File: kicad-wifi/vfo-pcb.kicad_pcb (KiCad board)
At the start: 2 copper layers, 108.4 x 79.9 mm, 110 parts, among them J1 Rotery Encoder1, J10 Link-out 1-2, J11 Link-out 1-0, J12 Link-out 2-0, J13 Link-out 2-2, J14 Link-out 2-1, J15 Link-out 1-1, J16 JTAG, J17 I2C, J2 Rotery Encoder2, J3 Analog in 3-6, J4 RxTx, J5 V12, J6 ESP32L, J7 ESP32R, J8 ILI9341, J9 Conn_01x07_Female, Q1 BFR92, Q2 BFR92, Q3 BFR92, Q4 BFR92, Q5 BFR92, Q6 BFR92, SW1 Rotary_Encoder_Switch, U1 AMS1117, U2 LM2576HVS-ADJ, U3 Si5351A-B-GT, U4 Si5351A-B-GT, U5 PCF8574ATS, Y1 Crystal, Y2 Crystal

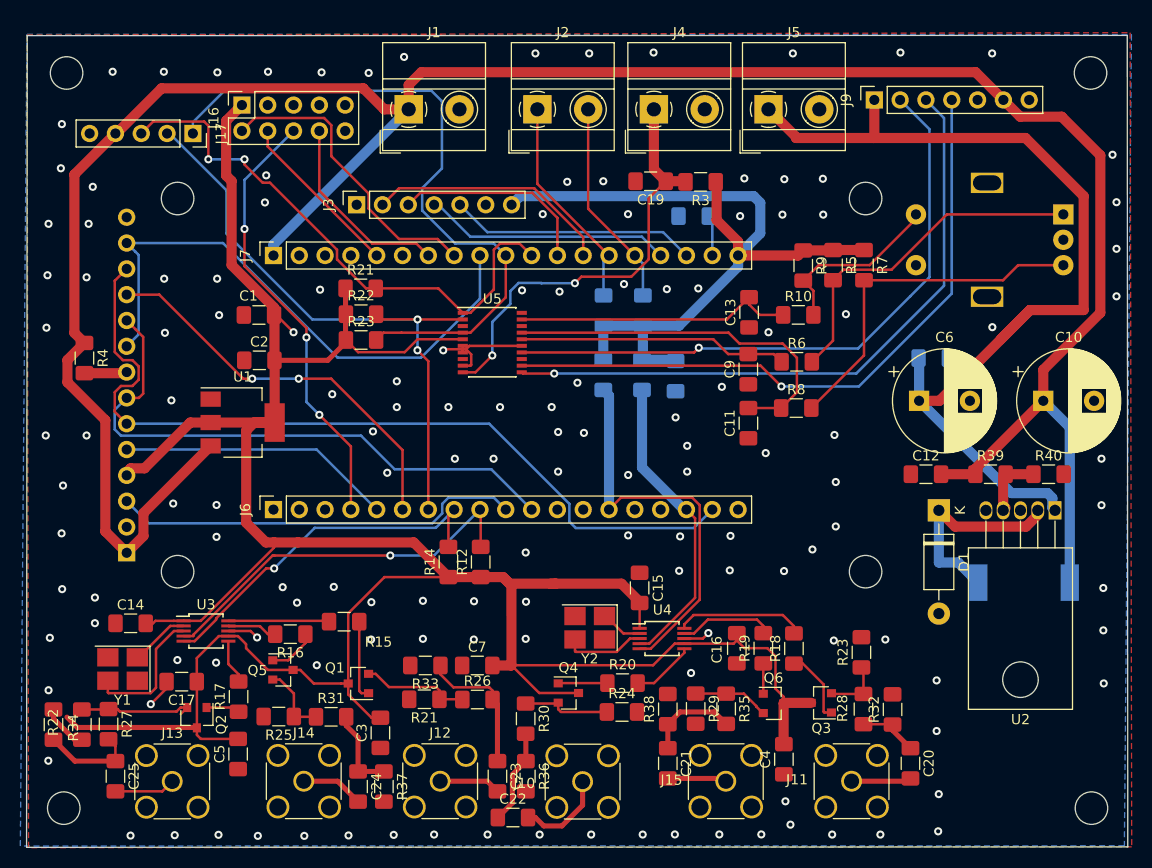
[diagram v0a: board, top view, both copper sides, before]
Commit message: 4 layer PCB
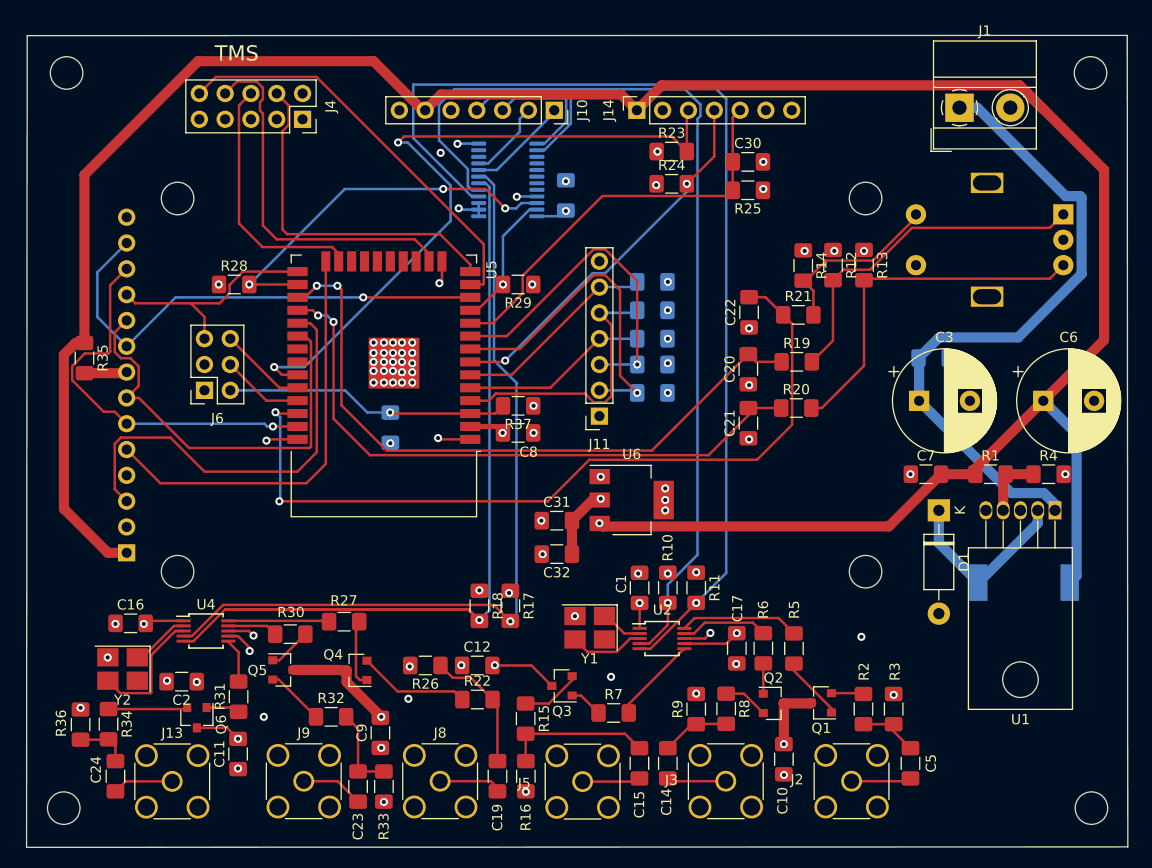
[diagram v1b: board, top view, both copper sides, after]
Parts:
- removed the C18 at (106.2, 85.9)
- removed the C2 at (65.2, 84.3)
- removed the J1 at (79.9, 59.6)
- removed J16: JTAG, Connector_PinSocket_2.54mm:PinSocket_2x05_P2.54mm_Vertical
- removed the J2 at (92.6, 59.6)
- removed J7: ESP32R, Connector_PinSocket_2.54mm:PinSocket_1x19_P2.54mm_Vertical
- removed the J9 at (125.7, 58.7)
- removed the R21 at (75.2, 77.2)
- removed the R21 at (81.5, 117.7)
- removed the R22 at (47.8, 120.1)
- removed the R23 at (75.2, 82.3)
- removed the R23 at (124.5, 113.0)
- removed the R24 at (100.9, 118.9)
- removed the R25 at (67.1, 119.3)
- removed the R32 at (127.5, 118.7)
- removed R38: 150, Resistor_SMD:R_1206_3216Metric_Pad1.42x1.75mm_HandSolder
- removed the U1 at (63.6, 90.4)
- added C13: 100n, Capacitor_SMD:C_1206_3216Metric_Pad1.42x1.75mm_HandSolder, B.Cu at (95.4, 68.1)
- added C25: 100n, Capacitor_SMD:C_1206_3216Metric_Pad1.42x1.75mm_HandSolder, B.Cu at (103.9, 76.6)
- added C26: 100n, Capacitor_SMD:C_1206_3216Metric_Pad1.42x1.75mm_HandSolder, B.Cu at (103.9, 79.4)
- added C27: 100n, Capacitor_SMD:C_1206_3216Metric_Pad1.42x1.75mm_HandSolder, B.Cu at (103.9, 82.2)
- added C28: 100n, Capacitor_SMD:C_1206_3216Metric_Pad1.42x1.75mm_HandSolder, B.Cu at (103.9, 87.5)
- added C29: 100n, Capacitor_SMD:C_1206_3216Metric_Pad1.42x1.75mm_HandSolder, B.Cu at (103.9, 84.7)
- added C31: 100n, Capacitor_SMD:C_1206_3216Metric_Pad1.42x1.75mm_HandSolder, F.Cu at (94.5, 100.1)
- added C32: 10u, Capacitor_SMD:C_1206_3216Metric_Pad1.42x1.75mm_HandSolder, F.Cu at (94.5, 103.4)
- added J14: Encoders, Connector_PinSocket_2.54mm:PinSocket_1x07_P2.54mm_Vertical, F.Cu at (102.4, 59.7)
- added R3: 68, Resistor_SMD:R_1206_3216Metric_Pad1.42x1.75mm_HandSolder, F.Cu at (127.6, 118.6)
- added R37: 1k, Resistor_SMD:R_1206_3216Metric_Pad1.42x1.75mm_HandSolder, F.Cu at (90.7, 88.8)
- added R9: 68, Resistor_SMD:R_1206_3216Metric_Pad1.42x1.75mm_HandSolder, F.Cu at (108.2, 118.6)
- added U3: TCA9548APWR, Package_SO:TSSOP-24_4.4x7.8mm_P0.65mm, B.Cu at (89.7, 66.5)
- added U6: LM1117-3.3, Package_TO_SOT_SMD:SOT-223-3_TabPin2, F.Cu at (101.9, 98.0)
- C20: renamed from C9; value 10n -> 100n
- C21: renamed from C11; value 10n -> 100n
- C22: renamed from C13; value 10n -> 100n
- J10: renamed from J17; footprint Connector_PinSocket_2.54mm:PinSocket_1x05_P2.54mm_Vertical -> Connector_PinSocket_2.54mm:PinSocket_1x07_P2.54mm_Vertical
- J4: value RxTx -> Jtag; footprint TerminalBlock_MetzConnect:TerminalBlock_MetzConnect_Type011_RT05502HBWC_1x02_P5.00mm_Horizontal -> Connector_PinSocket_2.54mm:PinSocket_2x05_P2.54mm_Vertical
- J6: value ESP32L -> Prog; footprint Connector_PinSocket_2.54mm:PinSocket_1x19_P2.54mm_Vertical -> Connector_PinSocket_2.54mm:PinSocket_2x03_P2.54mm_Vertical
- R10: renamed from R11; moved to F.Cu
- R11: renamed from R13; moved to F.Cu
- R15: renamed from R30; value 33 -> 200
- R16: renamed from R36; value 150 -> 68
- R2: renamed from R28; value 33 -> 200
- R23: renamed from R1; moved to F.Cu
- R24: renamed from R2; moved to F.Cu
- R29: value 150 -> 2.2k
- R8: renamed from R35; value 33 -> 200
- U5: value PCF8574ATS -> ESP32-WROOM-32D; footprint Package_SO:SSOP-20_4.4x6.5mm_P0.65mm -> RF_Module:ESP32-WROOM-32
- moved R29 45.2 mm to (90.7, 76.8), turned to 180 degrees
- moved C18 36.4 mm to (78.1, 90.9), turned to 270 degrees
- moved J10 35.6 mm to (94.2, 59.7)
- moved J4 34.6 mm to (69.5, 60.6), turned to 270 degrees
- moved J11 31.7 mm to (98.7, 89.8), turned to 180 degrees
- moved C8 28.0 mm to (90.7, 91.4), turned to 0 degrees
- moved R11 22.9 mm to (108.2, 106.7)
- moved R10 21.1 mm to (105.4, 106.7)
- moved J1 18.8 mm to (134.1, 59.4)
- moved R23 15.9 mm to (105.8, 63.8), turned to 0 degrees
- moved R24 14.2 mm to (105.8, 66.9), turned to 0 degrees
- moved J6 13.6 mm to (59.8, 87.2), turned to 180 degrees
- moved C15 13.5 mm to (102.6, 124.0), turned to 270 degrees
- moved R28 12.8 mm to (62.7, 76.8)
- moved U5 10.7 mm to (77.5, 83.8), turned to 180 degrees
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- renumbered C15 to C1, C4 to C10, C5 to C11, C7 to C12, C21 to C14, C22 to C15, C14 to C16, C16 to C17, C26 to C18, C23 to C19, C17 to C2, C24 to C23, C25 to C24, C6 to C3, C19 to C30, C8 to C4, C20 to C5, C10 to C6, C12 to C7, C1 to C8, C3 to C9, J5 to J1, J3 to J11, J8 to J12, J11 to J2, J15 to J3, J10 to J5, J12 to J8, J14 to J9, Q3 to Q1, Q6 to Q2, Q4 to Q3, Q1 to Q4, Q2 to Q6, R39 to R1, R5 to R12, R7 to R13, R9 to R14, R12 to R17, R14 to R18, R6 to R19, R8 to R20, R10 to R21, R26 to R22, R3 to R25, R33 to R26, R15 to R27, R22 to R28, R16 to R30, R17 to R31, R31 to R32, R37 to R33, R27 to R34, R4 to R35, R34 to R36, R40 to R4, R18 to R5, R19 to R6, R20 to R7, U2 to U1, U4 to U2, U3 to U4, Y2 to Y1, Y1 to Y2
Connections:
- C1 pad 2: V33a -> V33
- C10 pad 2: V33a -> V33
- C11 pad 2: V33a -> V33
- C12 pad 2: V33a -> V33
- C16 pad 2: V33a -> V33
- C17 pad 1: V33a -> V33
- C18 pad 1: Net-(C26-Pad1) -> EN
- C2 pad 1: V33a -> V33
- C8 pad 1: V33a -> V33
- C9 pad 2: V33a -> V33
- J10 pad 1: SDA -> SDA_3
- J10 pad 2: SCL -> SCL_3
- J10 pad 3: INT -> SDA_4
- J10 pad 4: Vcc -> SCL_4
- J10 pad 5: GND -> Net-(J10-Pad5)
- J11 pad 6: Net-(J3-Pad6) -> A5P
- J12 pad 4: V33a -> V33
- J4 pad 1: RXTX -> GND
- J4 pad 2: GND -> Net-(J4-Pad2)
- J6 pad 1: Net-(J6-Pad1) -> V33
- J6 pad 2: Net-(J6-Pad2) -> EN
- J6 pad 3: Net-(J6-Pad3) -> GND
- J6 pad 4: GPIO15 -> TXD0
- J6 pad 5: DC -> T_CS
- J6 pad 6: T_CS -> RXD0
- Q1 pad 3: V33a -> V33
- Q2 pad 2: Net-(Q6-Pad2) (its old number) -> Net-(Q2-Pad2)
- Q2 pad 3: V33a -> V33
- Q3 pad 3: V33a -> V33
- Q4 pad 3: V33a -> V33
- Q5 pad 3: V33a -> V33
- Q6 pad 3: V33a -> V33
- R17 pad 1: V33a -> V33
- R18 pad 1: V33a -> V33
- R28 pad 1: V33a -> V33
- R29 pad 1: Net-(Q6-Pad2) (its old number) -> V33
- R29 pad 2: GND -> SDA
- R8 pad 1: Net-(Q6-Pad2) (its old number) -> Net-(Q2-Pad2)
- U2 pad 1: V33a -> V33
- U2 pad 7: V33a -> V33
- U4 pad 1: V33a -> V33
- U4 pad 7: V33a -> V33
- U5 pad 1: INT -> GND
- U5 pad 11: RCLK_2 -> SDA
- U5 pad 12: SCLK_2 -> SDO
- U5 pad 13: Net-(U5-Pad13) -> GPIO14
- U5 pad 14: SER_2 -> GPIO12
- U5 pad 16: R1_2a -> GPIO13
- U5 pad 17: R2_2a -> Net-(U5-Pad17)
- U5 pad 19: R3_2a -> Net-(U5-Pad19)
- U5 pad 2: SCL -> V33
- U5 pad 3: Net-(U5-Pad3) -> EN
- U5 pad 4: SDA -> A4P
- U5 pad 5: V33a -> A3P
- U5 pad 6: GND -> A5P
- U5 pad 7: GND -> R2
- U5 pad 8: Net-(U5-Pad8) -> A1P
- U5 pad 9: GND -> A2P
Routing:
- net V33a: track 277.3 -> 0.00 mm, vias 1 -> 0
- net SCLK_2: track 66.0 -> 0.00 mm, vias 1 -> 0
- net SDA_1: track 38.9 -> 103.7 mm, vias 0 -> 1
- net SDA_2: track 36.0 -> 100.6 mm
- net RCLK_2: track 64.2 -> 0.00 mm, vias 1 -> 0
- net SCL_1: track 30.1 -> 93.5 mm, vias 0 -> 1
- net SER_2: track 61.9 -> 0.00 mm, vias 1 -> 0
- net INT: track 55.1 -> 0.00 mm, vias 2 -> 0
- net SDA: track 67.6 -> 13.4 mm, vias 0 -> 1
- net R3_2a: track 27.8 -> 80.0 mm, vias 0 -> 2
- net R1: track 20.5 -> 69.7 mm, vias 0 -> 2
- net SDI: track 83.0 -> 38.6 mm, vias 0 -> 1
- net SCL_2: track 38.1 -> 80.0 mm
- net R1_2a: track 26.5 -> 65.9 mm, vias 0 -> 2
- net V12V: track 96.2 -> 65.1 mm
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- added copper zone on IGND, net GND
- added copper zone on V33, net V33
- removed copper zone on B.Cu, net GND
- removed copper zone on F.Cu, net GND
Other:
- copper layers 2 -> 4
- board text added: "TMS"

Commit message: band select fixes
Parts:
- added C33: 100n, Capacitor_SMD:C_1206_3216Metric_Pad1.42x1.75mm_HandSolder, B.Cu at (47.1, 106.3)
- added J7: I2C, Connector_PinSocket_2.54mm:PinSocket_1x07_P2.54mm_Vertical, F.Cu at (108.8, 74.5)
- C8: value 10u -> 100n
- R35: moved to B.Cu
- moved R35 2.99 mm to (47.4, 87.0), turned to 90 degrees
- moved C20 2.25 mm to (115.5, 85.8)
- moved C21 2.25 mm to (115.5, 91.1)
- moved R19 2.25 mm to (120.3, 85.1)
- moved R21 2.25 mm to (120.4, 80.5)
- moved C22 2.25 mm to (115.6, 80.2)
- moved R20 2.25 mm to (120.2, 89.6)
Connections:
- U3 pad 3: GND -> V33
- U5 pad 31: Net-(U5-Pad31) -> GPIO19
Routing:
- net Vcc: track 252.6 -> 371.3 mm
- net GPIO19: track 0.00 -> 59.4 mm, vias 0 -> 3
- net A1P: track 33.0 -> 47.0 mm
- net R2_2a: track 61.4 -> 72.4 mm, vias 2 -> 0
- net R1_2a: track 65.9 -> 75.4 mm, vias 2 -> 0
- net V33: track 57.8 -> 66.2 mm, vias 28 -> 30
- net R3_2a: track 80.0 -> 87.9 mm
- net CS: track 42.7 -> 34.9 mm
- net A2P: track 33.2 -> 40.7 mm
- net SDI: track 38.6 -> 45.6 mm
- net R1: track 69.7 -> 64.3 mm
- net DC: track 41.7 -> 38.6 mm
- net A4P: track 27.3 -> 30.4 mm
- net R3_2: track 17.8 -> 20.7 mm
- net SCL_1: track 93.5 -> 96.0 mm
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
